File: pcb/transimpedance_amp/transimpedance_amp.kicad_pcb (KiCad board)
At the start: 2 copper layers, 40 x 50 mm, 37 parts, among them P1 CONN_01X05, P2 CONN_01X05, P3 CONN_01X05, P4 CONN_01X05, P5 CONN_01X05, P6 CONN_01X05, P7 CONN_01X05, P8 CONN_01X05, U1 AD8616

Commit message: Done with layouting so far.
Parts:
- added REF**: SolderWirePad_single_1mmDrill, Wire_Pads:SolderWirePad_single_1mmDrill, F.Cu at (182.1, 102.1)
- added REF**: SolderWirePad_single_1mmDrill, Wire_Pads:SolderWirePad_single_1mmDrill, F.Cu at (127.8, 122.9)
- added REF**: SolderWirePad_single_1mmDrill, Wire_Pads:SolderWirePad_single_1mmDrill, F.Cu at (178.8, 115.1)
- added REF**: SolderWirePad_single_1mmDrill, Wire_Pads:SolderWirePad_single_1mmDrill, F.Cu at (167.1, 120.9)
- added REF**: SolderWirePad_single_1mmDrill, Wire_Pads:SolderWirePad_single_1mmDrill, F.Cu at (173.5, 121.4)
- added REF**: SolderWirePad_single_1mmDrill, Wire_Pads:SolderWirePad_single_1mmDrill, F.Cu at (160.8, 120.7)
- added REF**: SolderWirePad_single_1mmDrill, Wire_Pads:SolderWirePad_single_1mmDrill, F.Cu at (148.6, 116.3)
- added REF**: SolderWirePad_single_1mmDrill, Wire_Pads:SolderWirePad_single_1mmDrill, F.Cu at (140.2, 120.1)
- added REF**: SolderWirePad_single_1mmDrill, Wire_Pads:SolderWirePad_single_1mmDrill, F.Cu at (134.1, 121.2)
- added REF**: MountingHole_3.2mm_M3_Pad, Mounting_Holes:MountingHole_3.2mm_M3_Pad, F.Cu at (182.0, 126.0)
- added TP4: TEST, Testpoints:TP_SMD_quadr_3mm, F.Cu at (133.6, 128.3)
- D2: value BPW34FA -> BPW34
- TP1, TP2, TP3: footprint Wire_Pads:SolderWirePad_single_1mmDrill -> Testpoints:TP_SMD_quadr_3mm
- moved REF** 134.2 mm to (112.0, 86.0)
- moved REF** 134.2 mm to (112.0, 126.0)
- moved REF** 131.2 mm to (182.0, 86.0)
- moved TP3 68.1 mm to (182.1, 97.3)
- moved D1 32.9 mm to (127.0, 106.0), turned to 270 degrees
- moved D2 15.7 mm to (135.4, 106.2)
- moved C10 13.9 mm to (125.7, 119.3)
- moved C6 13.9 mm to (151.1, 119.3)
- moved C7 13.9 mm to (142.3, 119.3)
- moved C8 13.9 mm to (135.9, 119.3)
- moved C9 13.9 mm to (129.6, 119.3)
- moved P7 13.9 mm to (150.5, 109.8)
- moved P8 13.9 mm to (150.5, 112.3)
- moved R10 13.9 mm to (123.2, 119.3)
- moved R6 13.9 mm to (148.6, 119.3)
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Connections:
- TP3 pad 1: Net-(P5-Pad1) -> GND
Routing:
- net Net-(P1-Pad1): track 15.5 -> 81.7 mm
- net Net-(P4-Pad1): track 27.3 -> 16.4 mm
- net Net-(P5-Pad1): track 26.7 -> 16.8 mm
- net Net-(P7-Pad1): track 18.9 -> 28.5 mm
- net +5V: track 9.15 -> 3.48 mm
- net Net-(C1-Pad1): track 48.5 -> 42.8 mm
- net Net-(D1-Pad1): track 7.01 -> 11.1 mm
- net Net-(C6-Pad1): track 20.9 -> 17.0 mm
- net Net-(C5-Pad1): track 19.7 -> 16.4 mm
- net Net-(C10-Pad1): track 48.1 -> 44.9 mm
- net Net-(C2-Pad1): track 37.6 -> 35.1 mm
- net Net-(C8-Pad1): track 28.7 -> 30.5 mm
- net Net-(C9-Pad1): track 37.6 -> 36.3 mm
- net Net-(D2-Pad1): track 6.89 -> 8.11 mm
- net Net-(C3-Pad1): track 28.7 -> 27.5 mm
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- added copper zone on B.Cu, net GND
- added copper zone on F.Cu, net GND
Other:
- board size 40 x 50 mm -> 80 x 50 mm

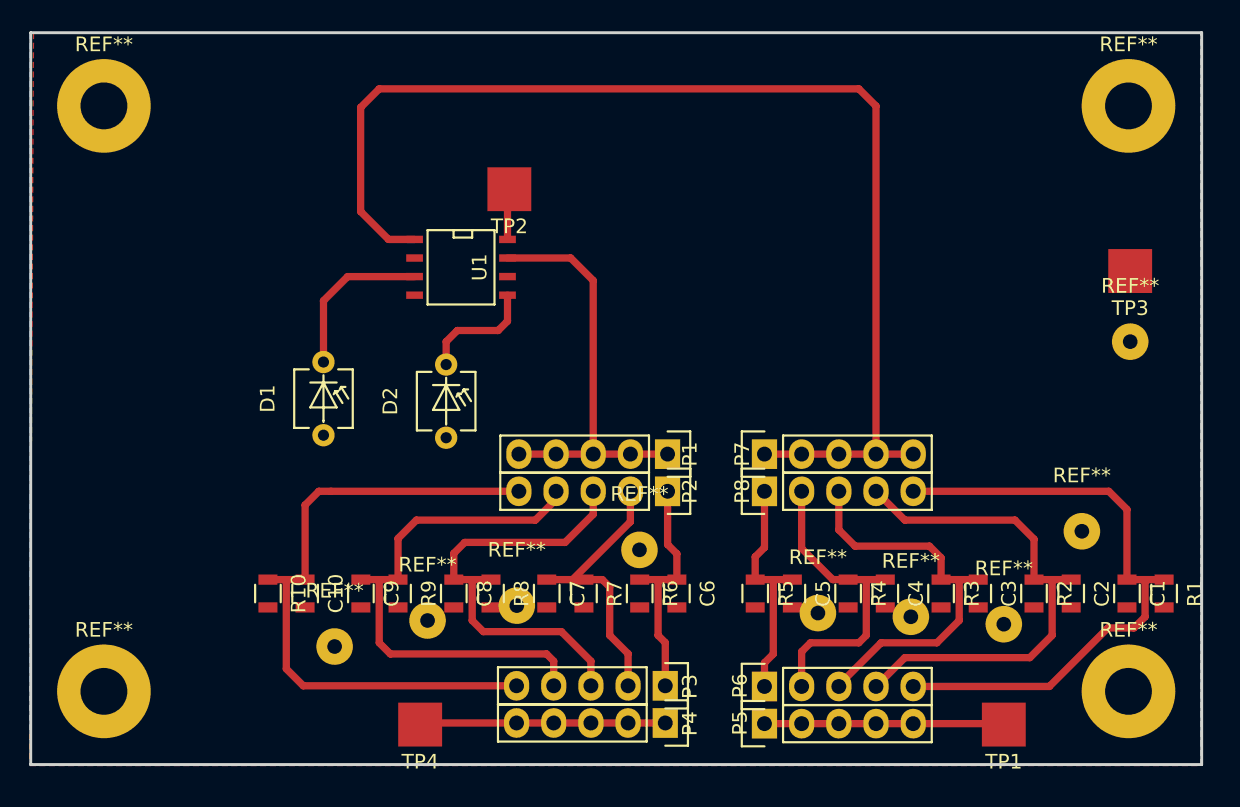
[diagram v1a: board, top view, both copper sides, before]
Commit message: Finished layout of transimpedance amplifier.
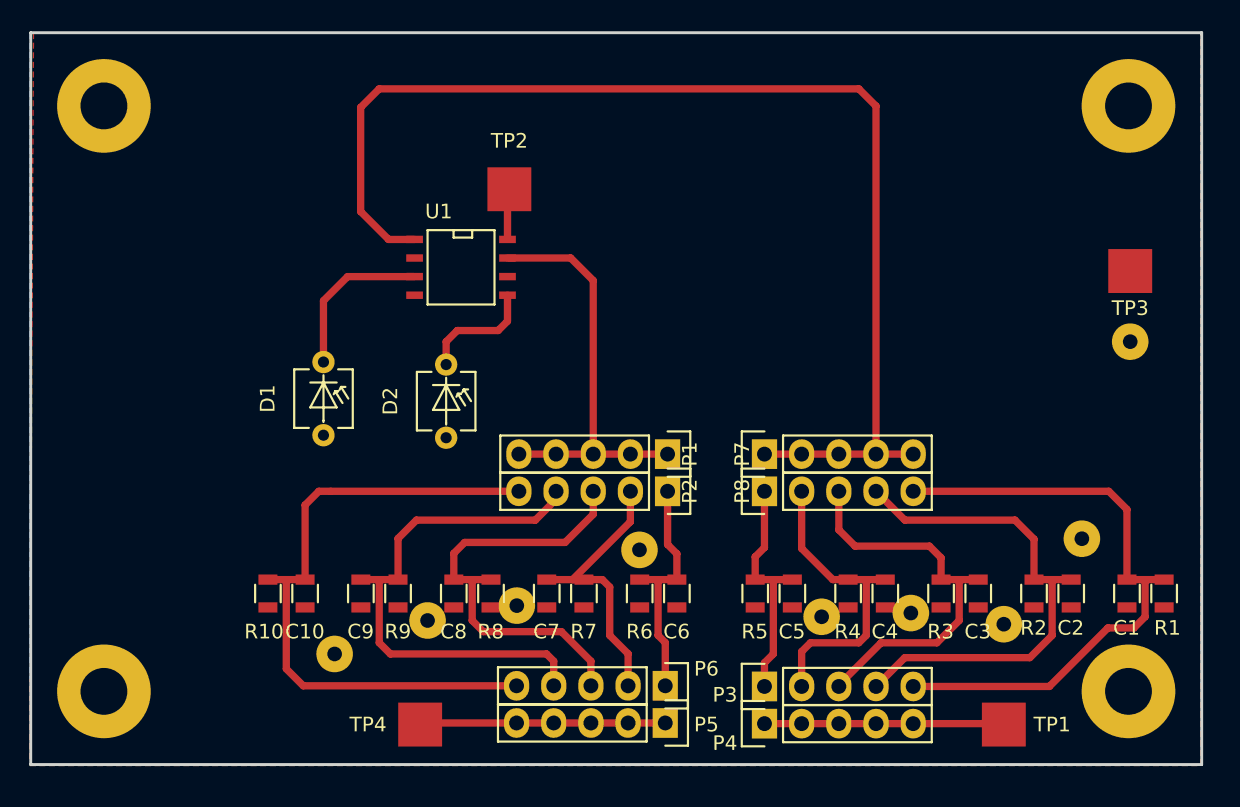
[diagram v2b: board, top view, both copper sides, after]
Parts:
- removed the REF** at (127.8, 122.9)
- removed the REF** at (178.8, 115.1)
- removed the REF** at (167.1, 120.9)
- removed the REF** at (160.8, 120.7)
- added REF**: SolderWirePad_single_1mmDrill, Wire_Pads:SolderWirePad_single_1mmDrill, F.Cu at (178.8, 115.6)
- added REF**: SolderWirePad_single_1mmDrill, Wire_Pads:SolderWirePad_single_1mmDrill, F.Cu at (167.1, 120.7)
- added REF**: SolderWirePad_single_1mmDrill, Wire_Pads:SolderWirePad_single_1mmDrill, F.Cu at (161.0, 120.9)
- added REF**: SolderWirePad_single_1mmDrill, Wire_Pads:SolderWirePad_single_1mmDrill, F.Cu at (127.8, 123.4)
